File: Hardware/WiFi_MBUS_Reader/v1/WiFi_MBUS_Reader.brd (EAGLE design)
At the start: 28.7 x 52.7 mm, 34 parts, among them U1 AP2112

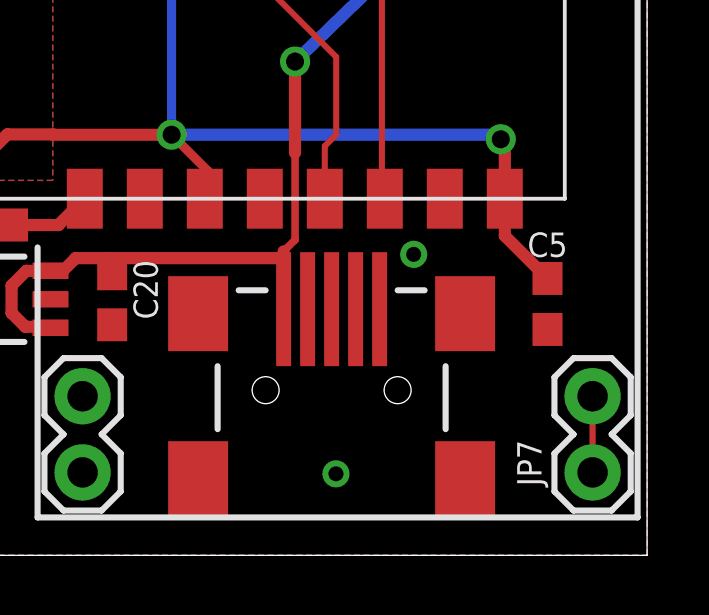
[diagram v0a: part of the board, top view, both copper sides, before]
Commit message: new MBUS reader hardware designs
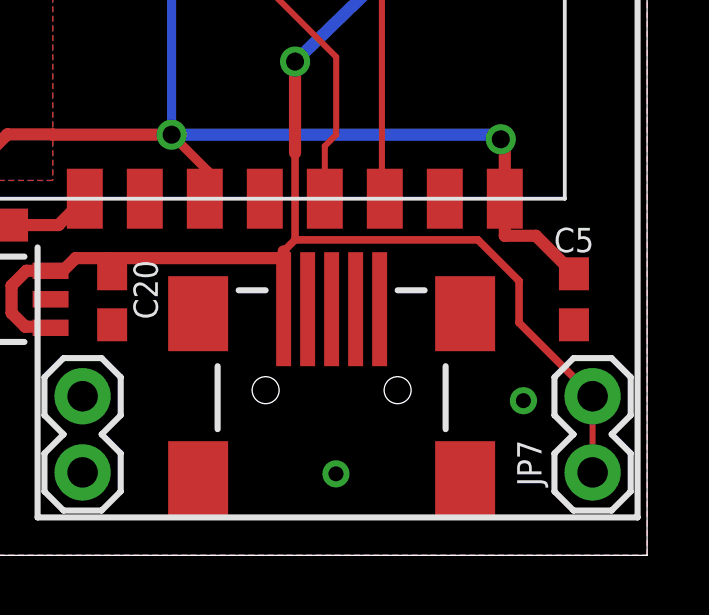
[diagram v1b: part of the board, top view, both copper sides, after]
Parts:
- moved C5 0.90 mm to (26.2, 8.53)
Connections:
- removed net 5V: JP7.1, JP7.2
- net 5V1: now also JP7.1, JP7.2
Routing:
- net 5V1: track 41.9 -> 57.8 mm
- net 5V: track 2.54 -> 0.00 mm
- net 3.3V: track 81.6 -> 82.4 mm
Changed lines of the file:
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@@
 <setting verticaltext="up"/>
 </settings>
-<grid distance="3" unitdist="mil" unit="mil" style="lines" multiple="1" display="yes" altdistance="0.635" altunitdist="mm" altunit="mm"/>
+<grid distance="12" unitdist="mil" unit="mil" style="lines" multiple="1" display="yes" altdistance="0.635" altunitdist="mm" altunit="mm"/>
 <layers>
 <layer number="1" name="Top" color="4" fill="1" visible="yes" active="yes"/>
@@
 <attribute name="NAME" x="21.4176" y="32.877" size="0.8128" layer="25" font="vector" ratio="20"/>
 </element>
-<element name="C5" library="resistor" package="C0603" value="100nF" x="25.3312" y="8.378" smashed="yes" rot="R90">
-<attribute name="NAME" x="24.6628" y="9.9462" size="0.8128" layer="25" font="vector" ratio="20"/>
+<element name="C5" library="resistor" package="C0603" value="100nF" x="26.2128" y="8.5344" smashed="yes" rot="R90">
+<attribute name="NAME" x="25.5444" y="10.1026" size="0.8128" layer="25" font="vector" ratio="20"/>
 </element>
 <element name="TX_LINK" library="SparkFun" package="SJ_2S-NO" value="SOLDERJUMPERNO" x="13.4112" y="31.3944" smashed="yes" rot="R180"/>
@@
 <via x="26.8148" y="27.71" extent="1-16" drill="0.5"/>
 <via x="26.8148" y="19.328" extent="1-16" drill="0.5"/>
-<via x="20.8712" y="10.0316" extent="1-16" drill="0.5"/>
+<via x="24.5288" y="5.1548" extent="1-16" drill="0.5"/>
 <via x="18.2804" y="2.7164" extent="1-16" drill="0.5"/>
 <via x="11.27" y="45.0836" extent="1-16" drill="0.5"/>
@@
 <contactref element="X7" pad="3"/>
 <wire x1="23.908" y1="11.8872" x2="23.908" y2="10.6512" width="0.4064" layer="1"/>
-<wire x1="23.908" y1="10.6512" x2="25.3312" y2="9.228" width="0.4064" layer="1"/>
 <contactref element="X1" pad="3"/>
 <contactref element="X2" pad="3"/>
@@
 <wire x1="5.7912" y1="11.034" x2="5.8168" y2="11.0084" width="0.4064" layer="1"/>
 <wire x1="12.8016" y1="27.1272" x2="7.62" y2="32.3088" width="0.3048" layer="16"/>
-</signal>
-<signal name="5V" class="1">
-<contactref element="JP7" pad="1"/>
-<contactref element="JP7" pad="2"/>
-<wire x1="26.8344" y1="5.3032" x2="26.8344" y2="2.7632" width="0.2032" layer="1"/>
+<wire x1="23.908" y1="10.6512" x2="24.946" y2="10.6512" width="0.4064" layer="1"/>
+<wire x1="24.946" y1="10.6512" x2="26.2128" y2="9.3844" width="0.4064" layer="1"/>
 </signal>
 <signal name="N$13">
@@
 <wire x1="16.9164" y1="13.4112" x2="16.9164" y2="10.5156" width="0.254" layer="1"/>
 <wire x1="16.9164" y1="10.5156" x2="16.5356" y2="10.1348" width="0.254" layer="1"/>
+<contactref element="JP7" pad="1"/>
+<contactref element="JP7" pad="2"/>
+<wire x1="26.8344" y1="5.3032" x2="26.8344" y2="2.7632" width="0.2032" layer="1"/>
+<wire x1="26.8344" y1="5.3032" x2="26.8344" y2="5.7792" width="0.254" layer="1"/>
+<wire x1="24.384" y1="7.7536" x2="24.384" y2="9.144" width="0.254" layer="1"/>
+<wire x1="24.384" y1="9.144" x2="23.0124" y2="10.5156" width="0.254" layer="1"/>
+<wire x1="16.9164" y1="10.5156" x2="23.0124" y2="10.5156" width="0.254" layer="1"/>
+<wire x1="24.384" y1="7.7536" x2="26.8344" y2="5.3032" width="0.254" layer="1"/>
 </signal>
 <signal name="DS18B20">
